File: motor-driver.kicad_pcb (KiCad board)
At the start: 2 copper layers, 0 parts

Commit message: Finish the initial placement, switch most of the parts to 0402.
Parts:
- added C1: 1nF, 100V, Capacitor_SMD:C_0402_1005Metric, F.Cu at (147.8, 78.8)
- added C10: 470nF, 50V, Capacitor_SMD:C_0603_1608Metric, B.Cu at (163.2, 70.2)
- added C11: 100nF, 50V, Capacitor_SMD:C_0402_1005Metric, B.Cu at (163.0, 76.0)
- added C12: 100nF, 50V, Capacitor_SMD:C_0402_1005Metric, B.Cu at (163.2, 68.4)
- added C13: 100nF, 50V, Capacitor_SMD:C_0402_1005Metric, B.Cu at (163.2, 73.0)
- added C14: 100nF, 50V, Capacitor_SMD:C_0402_1005Metric, B.Cu at (159.6, 66.8)
- added C15: 100nF, 50V, Capacitor_SMD:C_0402_1005Metric, B.Cu at (162.8, 66.8)
- added C16: 100nF, 50V, Capacitor_SMD:C_0402_1005Metric, B.Cu at (159.4, 76.0)
- added C17: 4.7uF, 16V, Capacitor_SMD:C_0603_1608Metric, B.Cu at (158.0, 72.6)
- added C18: 100nF, 50V, Capacitor_SMD:C_0402_1005Metric, B.Cu at (158.0, 71.4)
- added C19: 100nF, 50V, Capacitor_SMD:C_0402_1005Metric, B.Cu at (163.2, 72.0)
- added C2: 1nF, 100V, Capacitor_SMD:C_0402_1005Metric, F.Cu at (147.8, 81.2)
- added C20: 100nF, 50V, Capacitor_SMD:C_0402_1005Metric, B.Cu at (160.4, 76.0)
- added C21: 100nF, 50V, Capacitor_SMD:C_0402_1005Metric, B.Cu at (158.0, 66.4)
- added C22: 100nF, 50V, Capacitor_SMD:C_0402_1005Metric, B.Cu at (167.0, 76.2)
- added C23: 100nF, 100V, Capacitor_SMD:C_0603_1608Metric, B.Cu at (155.2, 89.2)
- added C24: 2.2uF, 50V, Capacitor_SMD:C_0805_2012Metric, B.Cu at (157.8, 83.8)
- added C25: 2.2uF, 50V, Capacitor_SMD:C_0805_2012Metric, B.Cu at (155.8, 83.8)
- added C26: 22nF, 100V, Capacitor_SMD:C_0603_1608Metric, B.Cu at (155.2, 91.6)
- added C27: 100nF, 100V, Capacitor_SMD:C_0603_1608Metric, B.Cu at (158.2, 91.6)
- added C28: 100nF, 100V, Capacitor_SMD:C_0603_1608Metric, B.Cu at (156.8, 89.2)
- added C29: 470nF, 16V, Capacitor_SMD:C_0603_1608Metric, F.Cu at (161.6, 80.8)
- added C3: 1nF, 100V, Capacitor_SMD:C_0402_1005Metric, F.Cu at (147.8, 83.6)
- added C30: 470nF, 16V, Capacitor_SMD:C_0603_1608Metric, F.Cu at (163.0, 86.4)
- added C31: 470nF, 16V, Capacitor_SMD:C_0603_1608Metric, F.Cu at (162.2, 92.4)
- added C32: 100nF, 50V, Capacitor_SMD:C_0402_1005Metric, B.Cu at (153.2, 83.8)
- added C33: 100nF, 50V, Capacitor_SMD:C_0402_1005Metric, B.Cu at (153.4, 86.8)
- added C34: 47uF, 63V, Capacitor_SMD:CP_Elec_6.3x7.7, B.Cu at (171.6, 68.8)
- added C35: 100nF, 50V, Capacitor_SMD:C_0402_1005Metric, B.Cu at (158.0, 68.4)
- added C36: 100nF, 50V, Capacitor_SMD:C_0402_1005Metric, B.Cu at (158.0, 67.4)
- added C37: 2.2uF, 100V, Capacitor_SMD:C_1206_3216Metric, B.Cu at (172.6, 80.5)
- added C38: 2.2uF, 100V, Capacitor_SMD:C_1206_3216Metric, B.Cu at (172.6, 85.5)
- added C39: 2.2uF, 100V, Capacitor_SMD:C_1206_3216Metric, B.Cu at (172.6, 90.6)
- added C4: 100pF, 50V, Capacitor_SMD:C_0402_1005Metric, F.Cu at (147.8, 71.0)
- added C40: 100nF, 50V, Capacitor_SMD:C_0402_1005Metric, B.Cu at (158.0, 70.4)
- added C5: 100pF, 50V, Capacitor_SMD:C_0402_1005Metric, F.Cu at (147.8, 73.6)
- added C6: 100pF, 50V, Capacitor_SMD:C_0402_1005Metric, F.Cu at (147.8, 76.2)
- added C7: 100nF, 50V, Capacitor_SMD:C_0402_1005Metric, B.Cu at (150.4, 78.6)
- added C8: 100nF, 50V, Capacitor_SMD:C_0402_1005Metric, B.Cu at (150.4, 73.2)
- added C9: 4.7uF, 16V, Capacitor_SMD:C_0603_1608Metric, B.Cu at (161.0, 66.8)
- added FB1: 600R, 1A, Resistor_SMD:R_0603_1608Metric, B.Cu at (165.0, 76.2)
- added J2: SIGNAL, Connector_PinHeader_2.54mm:PinHeader_2x10_P2.54mm_Vertical, B.Cu at (143.5, 67.6)
- added J3: PWR, Connector_PinHeader_2.54mm:PinHeader_1x10_P2.54mm_Vertical, B.Cu at (177.0, 67.6)
- added J4: RTMI, DF20EF-10DP-1V_52:HRS_DF20EF-10DP-1V(52), F.Cu at (171.0, 68.8)
- added Q4: SIZ322DT, SIZ322DT-T1-GE3:SIZ340DTT1GE3, F.Cu at (168.1, 81.2)
- added Q5: SIZ322DT, SIZ322DT-T1-GE3:SIZ340DTT1GE3, F.Cu at (168.1, 86.0)
- added Q6: SIZ322DT, SIZ322DT-T1-GE3:SIZ340DTT1GE3, F.Cu at (168.1, 90.8)
- added R1: 4.7K, %1, Resistor_SMD:R_0402_1005Metric, F.Cu at (146.8, 77.8)
- added R10: 4.7K, %1, Resistor_SMD:R_0402_1005Metric, B.Cu at (146.8, 70.0)
- added R11: 4.7K, %1, Resistor_SMD:R_0402_1005Metric, B.Cu at (146.8, 72.6)
- added R12: 4.7K, %1, Resistor_SMD:R_0402_1005Metric, B.Cu at (146.8, 75.2)
- added R13: 10K, %1, Resistor_SMD:R_0402_1005Metric, B.Cu at (162.0, 76.0)
- added R14: 0, Resistor_SMD:R_0402_1005Metric, B.Cu at (153.4, 87.8)
- added R15: 1.5K, %1, Resistor_SMD:R_0402_1005Metric, B.Cu at (153.2, 81.8)
- added R16: 4.7K, %1, Resistor_SMD:R_0402_1005Metric, B.Cu at (154.2, 83.8)
- added R17: 0, Resistor_SMD:R_0402_1005Metric, B.Cu at (152.8, 90.2)
- added R18: 47K, %1, Resistor_SMD:R_0402_1005Metric, B.Cu at (156.0, 68.4)
- added R19: 1K, %1, Resistor_SMD:R_0402_1005Metric, B.Cu at (158.0, 69.4)
- added R2: 4.7K, %1, Resistor_SMD:R_0402_1005Metric, F.Cu at (146.8, 80.2)
- added R20: 4.7K, %1, Resistor_SMD:R_0402_1005Metric, B.Cu at (156.0, 73.4)
- added R21: 4.7K, %1, Resistor_SMD:R_0402_1005Metric, B.Cu at (158.0, 73.8)
- added R22: 4.7K, %1, Resistor_SMD:R_0402_1005Metric, F.Cu at (151.4, 69.8)
- added R23: 4.7K, %1, Resistor_SMD:R_0402_1005Metric, F.Cu at (150.4, 69.8)
- added R3: 4.7K, %1, Resistor_SMD:R_0402_1005Metric, F.Cu at (146.8, 82.6)
- added R30: 22, %1, Resistor_SMD:R_0402_1005Metric, B.Cu at (168.1, 82.0)
- added R31: 22, %1, Resistor_SMD:R_0402_1005Metric, B.Cu at (168.1, 80.2)
- added R32: 22, %1, Resistor_SMD:R_0402_1005Metric, B.Cu at (168.1, 86.8)
- added R33: 22, %1, Resistor_SMD:R_0402_1005Metric, B.Cu at (168.1, 85.0)
- added R34: 22, %1, Resistor_SMD:R_0402_1005Metric, B.Cu at (168.1, 91.6)
- added R35: 22, %1, Resistor_SMD:R_0402_1005Metric, B.Cu at (168.1, 89.8)
- added R36: 0.033, %1, 1W, Resistor_SMD:R_1206_3216Metric, F.Cu at (172.6, 82.5)
- added R37: 0.033, %1, 1W, Resistor_SMD:R_1206_3216Metric, F.Cu at (172.6, 80.2)
- added R38: 0.033, %1, 1W, Resistor_SMD:R_1206_3216Metric, F.Cu at (172.6, 85.0)
- added R39: 0.033, %1, 1W, Resistor_SMD:R_1206_3216Metric, F.Cu at (172.6, 87.2)
- added R4: 4.7K, %1, Resistor_SMD:R_0402_1005Metric, B.Cu at (146.8, 77.8)
- added R40: 0.033, %1, 1W, Resistor_SMD:R_1206_3216Metric, F.Cu at (172.6, 89.8)
- added R41: 0.033, %1, 1W, Resistor_SMD:R_1206_3216Metric, F.Cu at (172.6, 92.1)
- added R42: 10, %1, Resistor_SMD:R_0402_1005Metric, B.Cu at (172.6, 83.0)
- added R43: 10, %1, Resistor_SMD:R_0402_1005Metric, B.Cu at (172.6, 88.0)
- added R44: 10, %1, Resistor_SMD:R_0402_1005Metric, B.Cu at (172.6, 93.1)
- added R5: 4.7K, %1, Resistor_SMD:R_0402_1005Metric, B.Cu at (146.8, 80.2)
- added R6: 4.7K, %1, Resistor_SMD:R_0402_1005Metric, B.Cu at (146.8, 82.6)
- added R7: 1K, %1, Resistor_SMD:R_0402_1005Metric, F.Cu at (146.8, 70.0)
- added R8: 1K, %1, Resistor_SMD:R_0402_1005Metric, F.Cu at (146.8, 72.6)
- added R9: 1K, %1, Resistor_SMD:R_0402_1005Metric, F.Cu at (146.8, 75.2)
- added TH1: 10K, %1, Resistor_SMD:R_0603_1608Metric, B.Cu at (150.4, 69.8)
- added U1: TMC4671, TMC4671:QFN40P650X1050X90-77N, F.Cu at (160.6, 71.4)
- added U2: 74LVC3G17, Package_SO:VSSOP-8_2.3x2mm_P0.5mm, F.Cu at (150.4, 78.6)
- added U3: 74LVC3G17, Package_SO:VSSOP-8_2.3x2mm_P0.5mm, F.Cu at (150.4, 73.2)
- added U4: TMC6200, Package_QFP:TQFP-48-1EP_7x7mm_P0.5mm_EP5x5mm, F.Cu at (156.0, 86.6)
- added XTAL1: MC2016, 25MHz, MC2016:XTAL_MC2016K25_2X1P6_AVX, F.Cu at (166.2, 76.2)
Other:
- board outline added: 40 x 30 mm

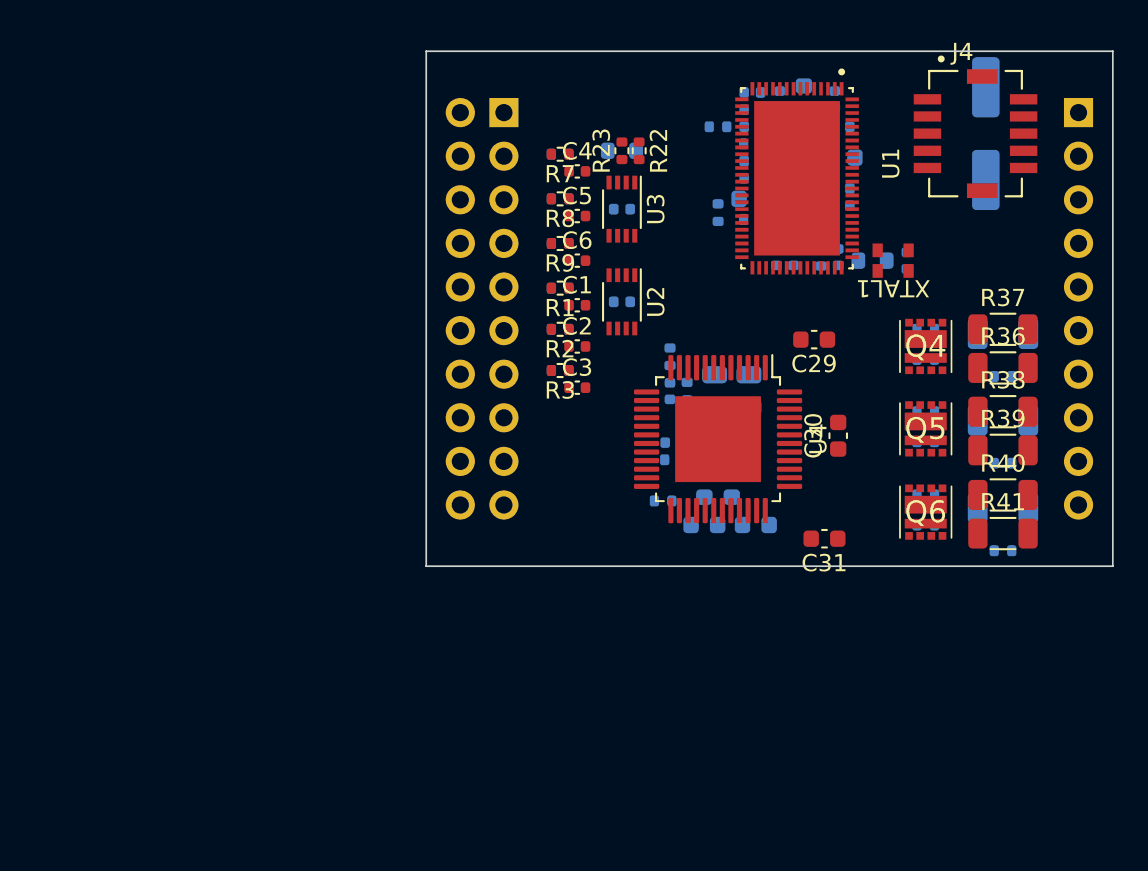
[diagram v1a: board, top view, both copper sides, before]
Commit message: Add signal RCs and debug LEDs.
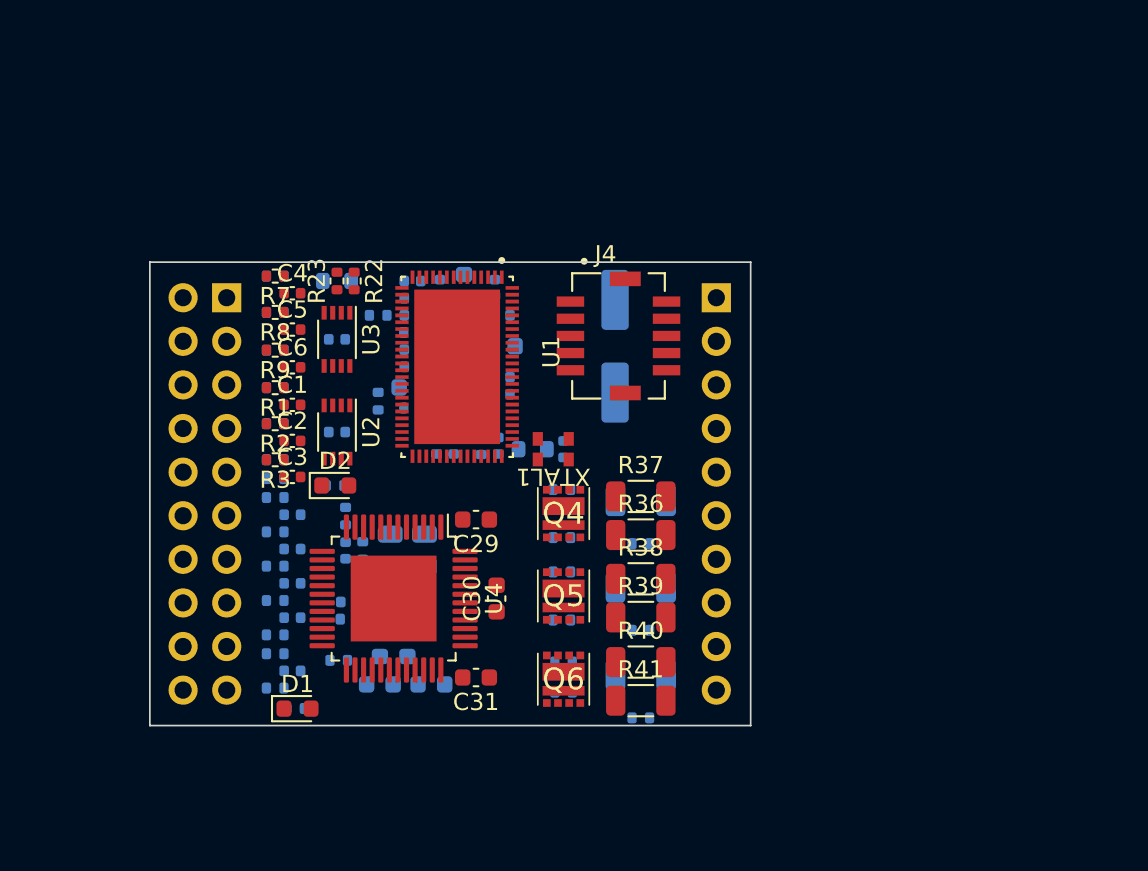
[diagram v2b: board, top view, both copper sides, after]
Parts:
- added C41: 100pF, 50V, Capacitor_SMD:C_0402_1005Metric, B.Cu at (131.2, 91.0)
- added C42: 100pF, 50V, Capacitor_SMD:C_0402_1005Metric, B.Cu at (131.2, 93.0)
- added C43: 100pF, 50V, Capacitor_SMD:C_0402_1005Metric, B.Cu at (131.2, 100.1)
- added C44: 100pF, 50V, Capacitor_SMD:C_0402_1005Metric, B.Cu at (131.2, 95.0)
- added C45: 100pF, 50V, Capacitor_SMD:C_0402_1005Metric, B.Cu at (131.2, 97.0)
- added D1: RED, LED_SMD:LED_0603_1608Metric, F.Cu at (131.5, 102.3)
- added D2: BLUE, LED_SMD:LED_0603_1608Metric, F.Cu at (133.7, 89.3)
- added R24: 270, %1, Resistor_SMD:R_0402_1005Metric, B.Cu at (130.2, 90.0)
- added R25: 150, %1, Resistor_SMD:R_0402_1005Metric, B.Cu at (130.2, 88.9)
- added R26: 150, %1, Resistor_SMD:R_0402_1005Metric, B.Cu at (130.2, 101.1)
- added R27: 270, %1, Resistor_SMD:R_0402_1005Metric, B.Cu at (130.2, 92.0)
- added R28: 270, %1, Resistor_SMD:R_0402_1005Metric, B.Cu at (130.2, 99.1)
- added R29: 270, %1, Resistor_SMD:R_0402_1005Metric, B.Cu at (130.2, 94.0)
- added R45: 270, %1, Resistor_SMD:R_0402_1005Metric, B.Cu at (130.2, 96.0)
- added R46: 150, %1, Resistor_SMD:R_0402_1005Metric, B.Cu at (130.2, 98.0)
- added R47: 220, %1, Resistor_SMD:R_0402_1005Metric, B.Cu at (131.4, 102.3)
- added R48: 100, %1, Resistor_SMD:R_0402_1005Metric, B.Cu at (133.7, 89.3)
- moved C34 24.9 mm to (150.0, 81.2)
- moved J4 23.9 mm to (150.2, 80.6)
- moved J3 23.7 mm to (155.9, 78.4)
- moved R32 23.6 mm to (146.9, 97.1), turned to 180 degrees
- moved R30 23.6 mm to (146.9, 92.3), turned to 180 degrees
- moved C37 23.2 mm to (151.5, 90.2)
- moved C38 23.2 mm to (151.5, 95.2)
- moved C39 23.2 mm to (151.5, 100.3)
- moved Q4 23.2 mm to (147.0, 90.9)
- moved Q5 23.2 mm to (147.0, 95.7)
- moved Q6 23.2 mm to (147.0, 100.6)
- moved R34 23.2 mm to (147.0, 101.3)
- moved R35 23.2 mm to (147.0, 99.6)
- moved R36 23.2 mm to (151.5, 92.2)
- moved R37 23.2 mm to (151.5, 89.9)
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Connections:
- J2 pad 11: /~{CS_CTRL} -> Net-(J2-Pin_11)
- J2 pad 13: /SPI_SCK -> Net-(J2-Pin_13)
- J2 pad 15: /SPI_MISO -> Net-(J2-Pin_15)
- J2 pad 17: /SPI_MOSI -> Net-(J2-Pin_17)
- J2 pad 19: unconnected-(J2-Pin_19-Pad19) -> Net-(J2-Pin_19)
- J2 pad 3: /CTRL_EN -> +3.3V
- J2 pad 5: /CTRL_STATUS -> Net-(J2-Pin_5)
- J2 pad 7: /DRV_FAULT -> Net-(J2-Pin_7)
- J2 pad 9: /~{CS_DRV} -> Net-(J2-Pin_9)
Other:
- board size 40 x 30 mm -> 35 x 27 mm
- copper layers 2 -> 4

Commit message: Start routing.
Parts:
- C26, C27, C37, C38, C39, R30, R31, R32, R33, R34, R35, R42, R43, R44: moved to F.Cu
- R36, R37, R38, R39, R40, R41: moved to B.Cu
- moved C32 16.5 mm to (129.9, 109.0)
- moved R48 16.2 mm to (117.7, 86.6)
- moved D2 16.2 mm to (117.7, 86.6)
- moved R16 13.6 mm to (135.3, 106.7)
- moved R15 13.5 mm to (134.0, 104.6), turned to 180 degrees
- moved R14 8.54 mm to (137.7, 105.0)
- moved C17 7.18 mm to (145.3, 82.5), turned to -90 degrees
- moved R17 6.18 mm to (131.8, 105.3), turned to -90 degrees
- moved R22 3.69 mm to (134.6, 73.7)
- moved R23 3.69 mm to (133.6, 73.7)
- moved TH1 3.69 mm to (133.6, 73.7)
- moved C24 3.26 mm to (141.2, 95.4)
- moved C25 3.26 mm to (139.2, 95.4)
- moved C33 2.94 mm to (137.3, 95.2)
- moved R42 2.93 mm to (154.4, 92.3), turned to 90 degrees
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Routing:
- net /SPI_MISO: track 0.00 -> 34.7 mm, vias 0 -> 2
- net /SPI_MOSI: track 0.00 -> 33.9 mm, vias 0 -> 3
- net /SPI_SCK: track 0.00 -> 32.5 mm, vias 0 -> 3
- net GND: track 0.00 -> 28.5 mm
- net /~{CS_CTRL}: track 0.00 -> 28.3 mm, vias 0 -> 3
- net /Controller/DRV_EN: track 0.00 -> 26.8 mm, vias 0 -> 2
- net /CUR_W: track 0.00 -> 24.9 mm, vias 0 -> 2
- net /CUR_U: track 0.00 -> 24.6 mm, vias 0 -> 2
- net /Controller/WL: track 0.00 -> 23.5 mm, vias 0 -> 2
- net /Controller/WH: track 0.00 -> 21.1 mm, vias 0 -> 2
- net /CTRL_STATUS: track 0.00 -> 20.4 mm, vias 0 -> 1
- net +24V: track 0.00 -> 19.2 mm
- net /Controller/VL: track 0.00 -> 18.1 mm, vias 0 -> 2
- net /Controller/VH: track 0.00 -> 17.2 mm, vias 0 -> 2
- net /Controller/UL: track 0.00 -> 15.8 mm, vias 0 -> 2
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- added copper zone on In1.Cu, net +24V
- added copper zone on In2.Cu, net GND

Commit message: Finish draft routing,
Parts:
- C19, C22, FB1, R48: moved to F.Cu
- R22, R23: moved to B.Cu
- moved TH1 21.9 mm to (148.2, 90.0), turned to -90 degrees
- moved C32 16.3 mm to (137.0, 94.3), turned to 180 degrees
- moved R22 14.9 mm to (141.8, 86.8), turned to 0 degrees
- moved D2 14.3 mm to (129.4, 94.8), turned to 90 degrees
- moved R16 13.9 mm to (137.1, 92.9)
- moved R18 13.5 mm to (150.0, 86.6), turned to 0 degrees
- moved R23 13.3 mm to (138.0, 86.2), turned to -90 degrees
- moved R48 12.6 mm to (129.0, 92.2), turned to -90 degrees
- moved R15 9.24 mm to (136.5, 95.7), turned to -90 degrees
- moved R17 7.56 mm to (134.4, 98.2)
- moved FB1 7.03 mm to (150.9, 88.0), turned to 180 degrees
- moved C17 6.40 mm to (139.0, 83.6), turned to 180 degrees
- moved R14 6.02 mm to (135.5, 99.4), turned to -90 degrees
- moved C16 5.70 mm to (140.0, 91.0), turned to 90 degrees
- moved C20 5.70 mm to (141.0, 91.0), turned to 90 degrees
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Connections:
- J2 pad 1: +3.3V -> +5V
- J2 pad 2: +5V -> unconnected-(J2-Pin_2-Pad2)
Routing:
- net GND: track 28.5 -> 62.2 mm, vias 0 -> 21
- net +3.3V: track 0.00 -> 30.7 mm, vias 0 -> 15
- net /CTRL_EN: track 1.00 -> 20.5 mm, vias 0 -> 3
- net /Controller/ADC_VM: track 0.00 -> 18.9 mm, vias 0 -> 1
- net +5V: track 0.00 -> 18.8 mm, vias 0 -> 1
- net Net-(R22-Pad2): track 0.00 -> 12.8 mm
- net /Driver/W_DRV: track 4.74 -> 16.6 mm, vias 0 -> 2
- net /Driver/U_DRV: track 4.92 -> 16.5 mm, vias 0 -> 2
- net /Driver/V_DRV: track 2.38 -> 13.4 mm, vias 0 -> 2
- net /Controller/DRV_EN: track 26.8 -> 37.3 mm
- net +24V: track 19.2 -> 29.6 mm, vias 0 -> 7
- net Net-(U1-AGPI_B): track 0.00 -> 10.1 mm, vias 0 -> 1
- net Net-(U1-~{RST}): track 0.00 -> 7.04 mm, vias 0 -> 1
- net +2V5: track 0.00 -> 6.66 mm, vias 0 -> 1
- net Net-(U4-VOFS/TEST): track 0.00 -> 5.02 mm, vias 0 -> 1
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- added copper zone on In1.Cu, net +3.3V
- added copper zone on In1.Cu, net +5V
- added copper zone on B.Cu, net GND
- added copper zone on In1.Cu, net GND

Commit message: Improve routing.
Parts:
- moved D1 4.08 mm to (129.4, 98.8), turned to -90 degrees
- moved R18 1.48 mm to (149.3, 87.9)
- moved FB1 1.08 mm to (150.0, 87.4), turned to -90 degrees
- moved R16 0.57 mm to (136.7, 92.5), turned to 180 degrees
- moved TH1 0.41 mm to (148.3, 90.4)
- moved C32 0.40 mm to (137.0, 94.7)
- moved R15 0.40 mm to (136.5, 96.1)
- moved C24 0.10 mm to (141.6, 95.8)
- moved C25 0.10 mm to (139.6, 95.8)
- moved C28 0.10 mm to (140.2, 98.3)
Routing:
- net GND: track 62.2 -> 39.9 mm, vias 21 -> 22
- net +24V: track 29.6 -> 7.85 mm, vias 7 -> 10
- net /U: track 10.0 -> 1.80 mm
- net /V: track 9.97 -> 1.91 mm
- net /W: track 9.66 -> 1.71 mm
- net /Driver/V_DRV: track 13.4 -> 8.20 mm, vias 2 -> 3
- net /Driver/U_DRV: track 16.5 -> 11.7 mm, vias 2 -> 3
- net /Driver/W_DRV: track 16.6 -> 12.2 mm, vias 2 -> 3
- net Net-(XTAL1-EN): track 3.60 -> 0.11 mm
- net Net-(D1-A): track 2.30 -> 5.69 mm
- net +3.3V: track 30.7 -> 33.9 mm
- net /ENC_A: track 11.4 -> 8.44 mm
- net Net-(U1-ENC_A): track 9.56 -> 6.72 mm
- net +5V: track 18.8 -> 16.1 mm, vias 1 -> 2
- net /Controller/DRV_EN: track 37.3 -> 35.3 mm
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- added copper zone on B.Cu, net +24V
- added copper zone on F.Cu, net +24V
- added copper zone on B.Cu, net /Driver/U_DRV
- added copper zone on F.Cu, net /Driver/U_DRV
- added copper zone on B.Cu, net /Driver/V_DRV
- added copper zone on F.Cu, net /Driver/V_DRV
- added copper zone on B.Cu, net /Driver/W_DRV
- added copper zone on F.Cu, net /Driver/W_DRV
- added copper zone on B.Cu, net /U
- added copper zone on B.Cu, net /V
- added copper zone on B.Cu, net /W
- added copper zone on F.Cu, net GND
- added copper zone on F.Cu, net Net-(XTAL1-EN)
